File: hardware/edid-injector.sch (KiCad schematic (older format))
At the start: 45 parts

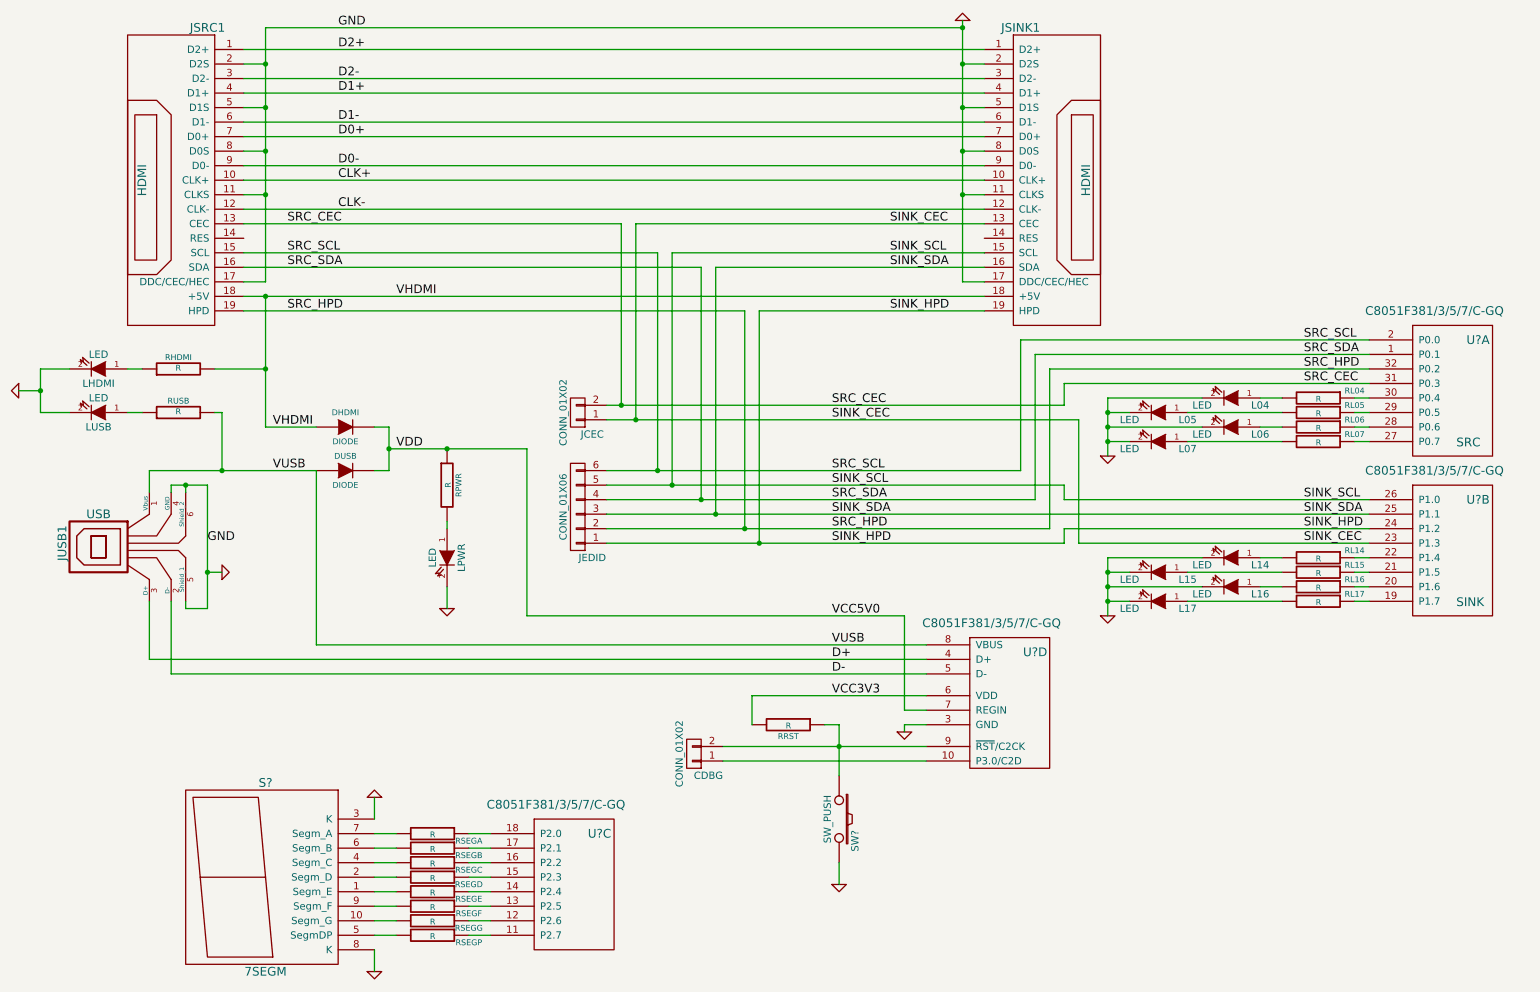
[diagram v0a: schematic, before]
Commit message: Temporary commit to allow John to take a look at the design.
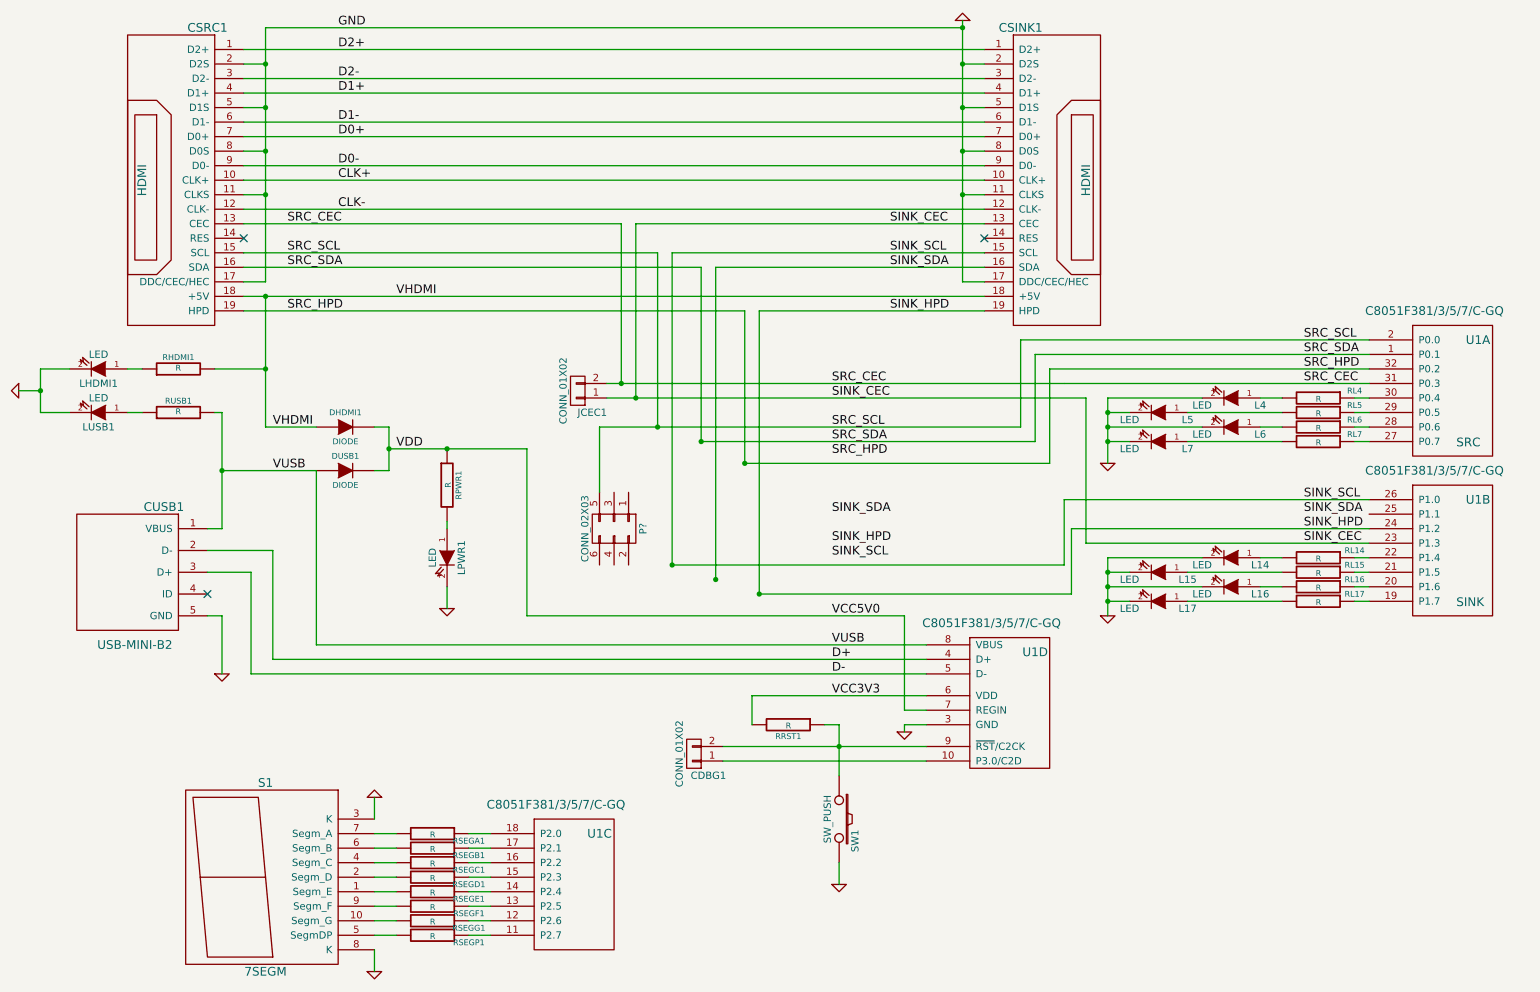
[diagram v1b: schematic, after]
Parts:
- removed JEDID: CONN_01X06, symbol CONN_01X06
- removed JUSB1: USB, symbol USB
- added CUSB1: USB-MINI-B2, micro-usb:micro-usb, symbol USB-MINI-B2
- added P?: CONN_02X03, symbol CONN_02X03
- CDBG1: renamed from CDBG; footprint (none) -> Pin_Headers:Pin_Header_Straight_1x02
- CSINK1: renamed from JSINK1; footprint (none) -> hdmi:hdmi
- CSRC1: renamed from JSRC1; footprint (none) -> hdmi:hdmi
- DHDMI1: renamed from DHDMI; footprint (none) -> sod323:sod323
- DUSB1: renamed from DUSB; footprint (none) -> sod323:sod323
- JCEC1: renamed from JCEC; footprint (none) -> Pin_Headers:Pin_Header_Straight_1x02
- L14, L15, L16, L17: footprint (none) -> LEDs:LED-0805
- L4: renamed from L04; footprint (none) -> LEDs:LED-0805
- L5: renamed from L05; footprint (none) -> LEDs:LED-0805
- L6: renamed from L06; footprint (none) -> LEDs:LED-0805
- L7: renamed from L07; footprint (none) -> LEDs:LED-0805
- LHDMI1: renamed from LHDMI; footprint (none) -> LEDs:LED-0805
- LPWR1: renamed from LPWR; footprint (none) -> LEDs:LED-0805
- LUSB1: renamed from LUSB; footprint (none) -> LEDs:LED-0805
- RHDMI1: renamed from RHDMI; footprint (none) -> Resistors_SMD:R_0402
- RL14, RL15, RL16, RL17: footprint (none) -> Resistors_SMD:R_0402
- RL4: renamed from RL04; footprint (none) -> Resistors_SMD:R_0402
- RL5: renamed from RL05; footprint (none) -> Resistors_SMD:R_0402
- RL6: renamed from RL06; footprint (none) -> Resistors_SMD:R_0402
- RL7: renamed from RL07; footprint (none) -> Resistors_SMD:R_0402
- RPWR1: renamed from RPWR; footprint (none) -> Resistors_SMD:R_0402
- RRST1: renamed from RRST; footprint (none) -> Resistors_SMD:R_0402
- RSEGA1: renamed from RSEGA; footprint (none) -> Resistors_SMD:R_0402
- RSEGB1: renamed from RSEGB; footprint (none) -> Resistors_SMD:R_0402
- RSEGC1: renamed from RSEGC; footprint (none) -> Resistors_SMD:R_0402
- RSEGD1: renamed from RSEGD; footprint (none) -> Resistors_SMD:R_0402
- RSEGE1: renamed from RSEGE; footprint (none) -> Resistors_SMD:R_0402
- RSEGF1: renamed from RSEGF; footprint (none) -> Resistors_SMD:R_0402
- RSEGG1: renamed from RSEGG; footprint (none) -> Resistors_SMD:R_0402
- RSEGP1: renamed from RSEGP; footprint (none) -> Resistors_SMD:R_0402
- RUSB1: renamed from RUSB; footprint (none) -> Resistors_SMD:R_0402
- S1: renamed from S?; footprint (none) -> Displays_7-Segment:7SegmentLED_SBC18-11EGWA
- SW1: renamed from SW?; footprint (none) -> Pin_Headers:Pin_Header_Angled_1x02
- U1: renamed from U?; footprint (none) -> QFP:lqfp32
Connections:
- net D+: now also CUSB1.2 (D-)
- net D-: now also CUSB1.3 (D+)
- net GND: now also CUSB1.5 (GND)
- net SINK_SDA: no longer U1.25 (P1.1)
- net SRC_SCL: now also P?.5 (P5)
- net VUSB: now also CUSB1.1 (VBUS)
- no-connect marks 0 -> 3
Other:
- moved on the sheet: JCEC1

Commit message: Fix schematic no-connects and some electrical rules
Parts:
- gave numbers to parts that had none: 1
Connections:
- net SINK_SDA: now also U1.25 (P1.1)
- no-connect marks 3 -> 8

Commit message: Update 7-segment footprint and add Digikey Ref.
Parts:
- P1: footprint (none) -> Pin_Headers:Pin_Header_Straight_2x03
- S1: footprint Displays_7-Segment:7SegmentLED_SBC18-11EGWA -> Sockets_DIP:DIP-10__300
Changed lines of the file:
@@
 LIBS:usb-mini-b
 LIBS:edid-injector-cache
-EELAYER 24 0
+EELAYER 25 0
 EELAYER END
 $Descr A4 11693 8268
@@
 F 0 "S1" H 2500 7250 60  0000 C CNN
 F 1 "7SEGM" H 2500 5950 60  0000 C CNN
-F 2 "Displays_7-Segment:7SegmentLED_SBC18-11EGWA" H 2500 6600 60  0001 C CNN
-F 3 "" H 2500 6600 60  0000 C CNN
+F 2 "Sockets_DIP:DIP-10__300" H 2500 6600 60  0001 C CNN
+F 3 "HDSP-303E" H 2500 6600 60  0000 C CNN
 	1    2500 6600
 	-1   0    0    -1
@@
 F 0 "P1" H 4900 4400 50  0000 C CNN
 F 1 "CONN_02X03" H 4900 4000 50  0000 C CNN
-F 2 "" H 4900 3000 60  0000 C CNN
+F 2 "Pin_Headers:Pin_Header_Straight_2x03" H 4900 3000 60  0001 C CNN
 F 3 "" H 4900 3000 60  0000 C CNN
 	1    4900 4200

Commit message: Fixing the EDID jumper.
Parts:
- renumbered P1 to JEDID1
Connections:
- net SINK_CEC: now also U1.26 (P1.0); no longer U1.23 (P1.3)
- net SINK_HPD: now also JEDID1.6 (P6), U1.23 (P1.3); no longer U1.24 (P1.2)
- net SINK_SCL: now also JEDID1.2 (P2), U1.25 (P1.1); no longer U1.26 (P1.0)
- net SINK_SDA: now also JEDID1.4 (P4), U1.24 (P1.2); no longer U1.25 (P1.1)
- net SRC_CEC: now also U1.2 (P0.0); no longer U1.31 (P0.3)
- net SRC_HPD: now also JEDID1.1 (P1), U1.31 (P0.3); no longer U1.32 (P0.2)
- net SRC_SCL: now also U1.1 (P0.1); no longer U1.2 (P0.0)
- net SRC_SDA: now also JEDID1.3 (P3), U1.32 (P0.2); no longer U1.1 (P0.1)
- no-connect marks 8 -> 3
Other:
- moved on the sheet: JCEC1, JEDID1
